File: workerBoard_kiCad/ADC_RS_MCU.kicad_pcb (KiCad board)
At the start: 4 copper layers, 165 x 40 mm, 80 parts, among them J1 1053141216, P2 Plug, P3 Plug, P4 Plug, U1 AD7768-4BSTZ, U10 ADA4841-2YRMZ-RL, U11 THVD8000DDFR, U2 DSC1001AI2-032.7680, U3 ADR435BRZ, U4 REG103UA-5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

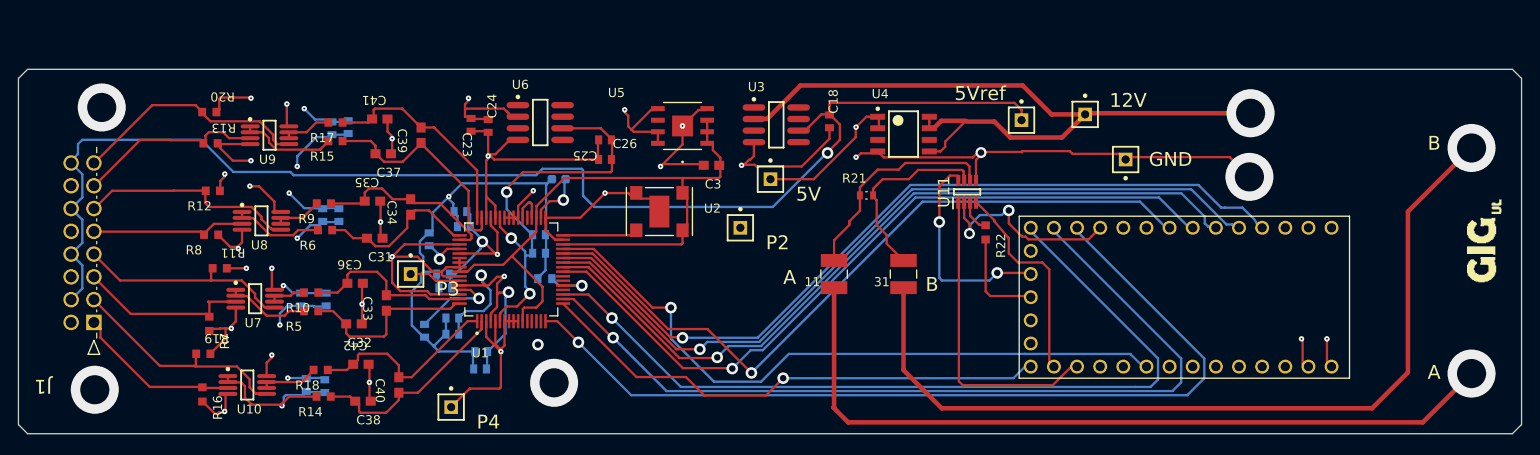
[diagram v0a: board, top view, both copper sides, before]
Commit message: Change the grid settings, must be 0.127 mm
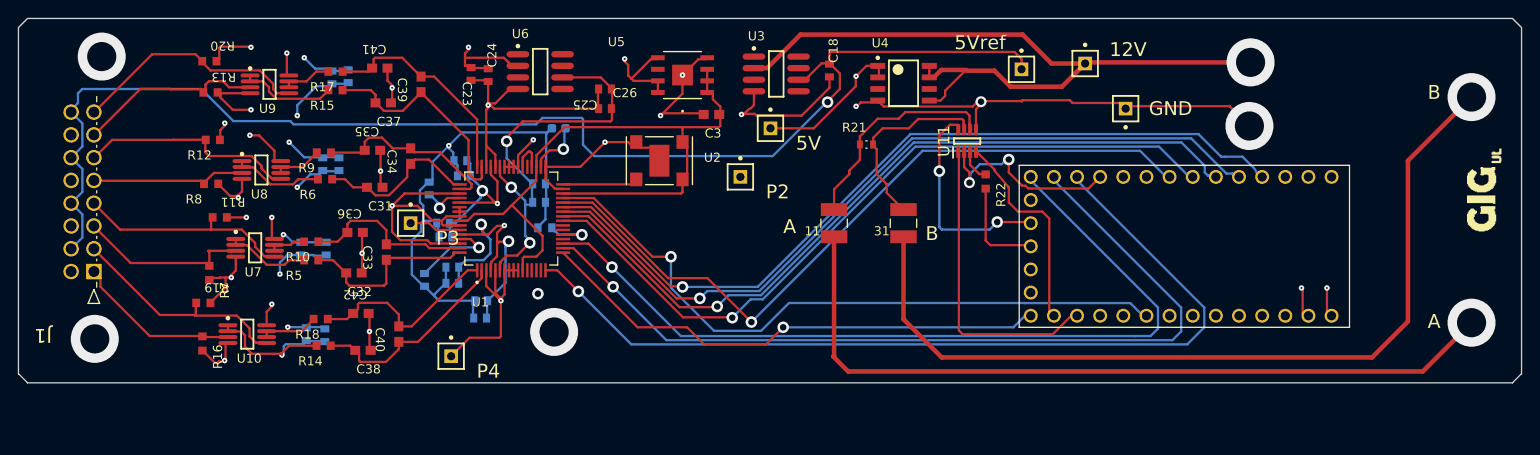
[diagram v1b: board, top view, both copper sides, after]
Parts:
- moved 5Vref 5.59 mm to (176.1, 85.0)
- moved C15 5.59 mm to (113.6, 106.7)
- moved C18 5.59 mm to (155.0, 85.1)
- moved C23 5.59 mm to (115.7, 85.5)
- moved C25 5.59 mm to (130.4, 89.3)
- moved C27 5.59 mm to (99.8, 104.7)
- moved C28 5.59 mm to (97.0, 104.7)
- moved C29 5.59 mm to (99.4, 95.4)
- moved C30 5.59 mm to (101.2, 95.4)
- moved C33 5.59 mm to (106.4, 105.1)
- moved C35 5.59 mm to (104.9, 93.9)
- moved C36 5.59 mm to (103.0, 102.9)
- moved C39 5.59 mm to (110.2, 86.7)
- moved C40 5.59 mm to (107.8, 114.1)
- moved C42 5.59 mm to (103.6, 111.8)
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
